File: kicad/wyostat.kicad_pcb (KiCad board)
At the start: 2 copper layers, 99.1 x 99.1 mm, 93 parts, among them J1 24 V AC IN, J10 Y2, J11 G, J12 W1, J13 USB_microAB, J14 W2, J15 Conn_Spare, J16 5V_SEL, J2 OUT1, J3 OUT2, J4 OUT3, J5 I2C_ext1, J6 RH, J7 RC, J8 C, J9 Y1, Q1 BTA204S, Q2 BTA204S, Q3 BTA204S, U1 MOC3063M, U2 MOC3063M, U3 MOC3063M, U4 Wemos-Lolin, U5 MAX17502FATB+T, U6 DS3231N

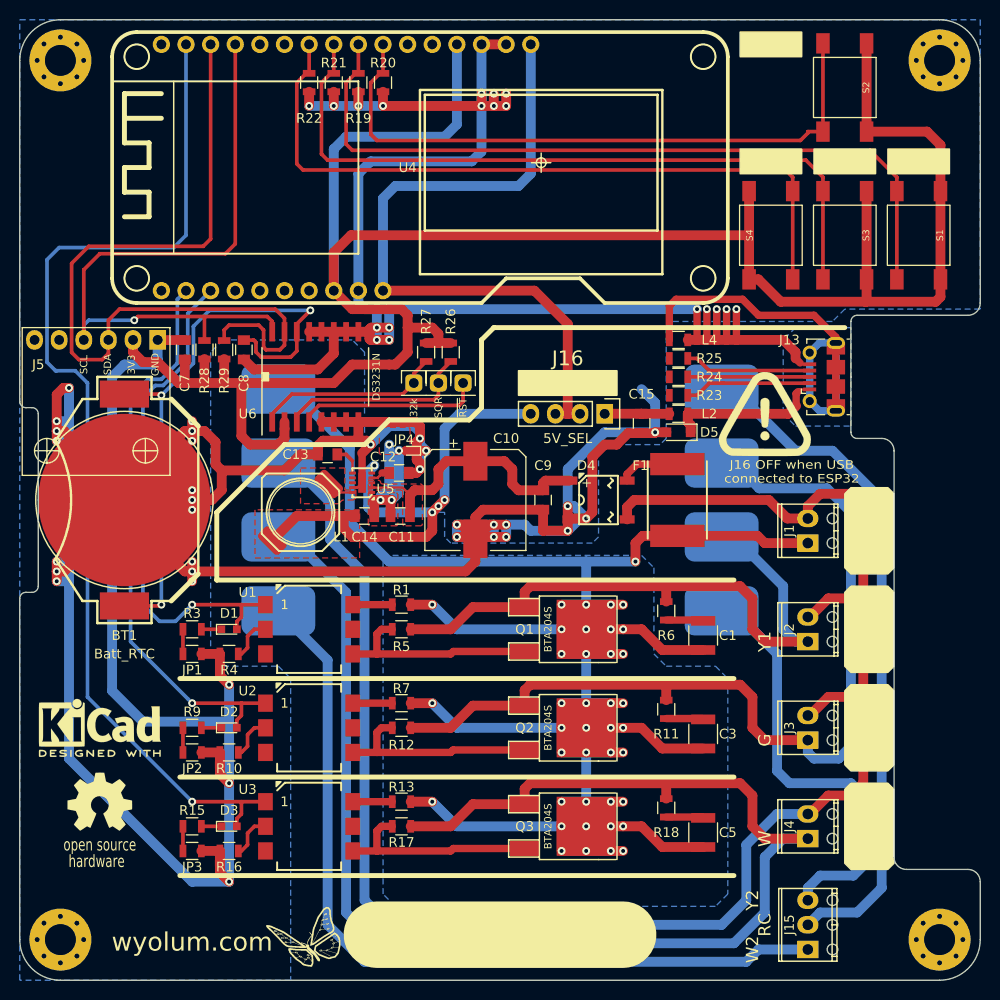
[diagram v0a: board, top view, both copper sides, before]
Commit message: prettified silk legend
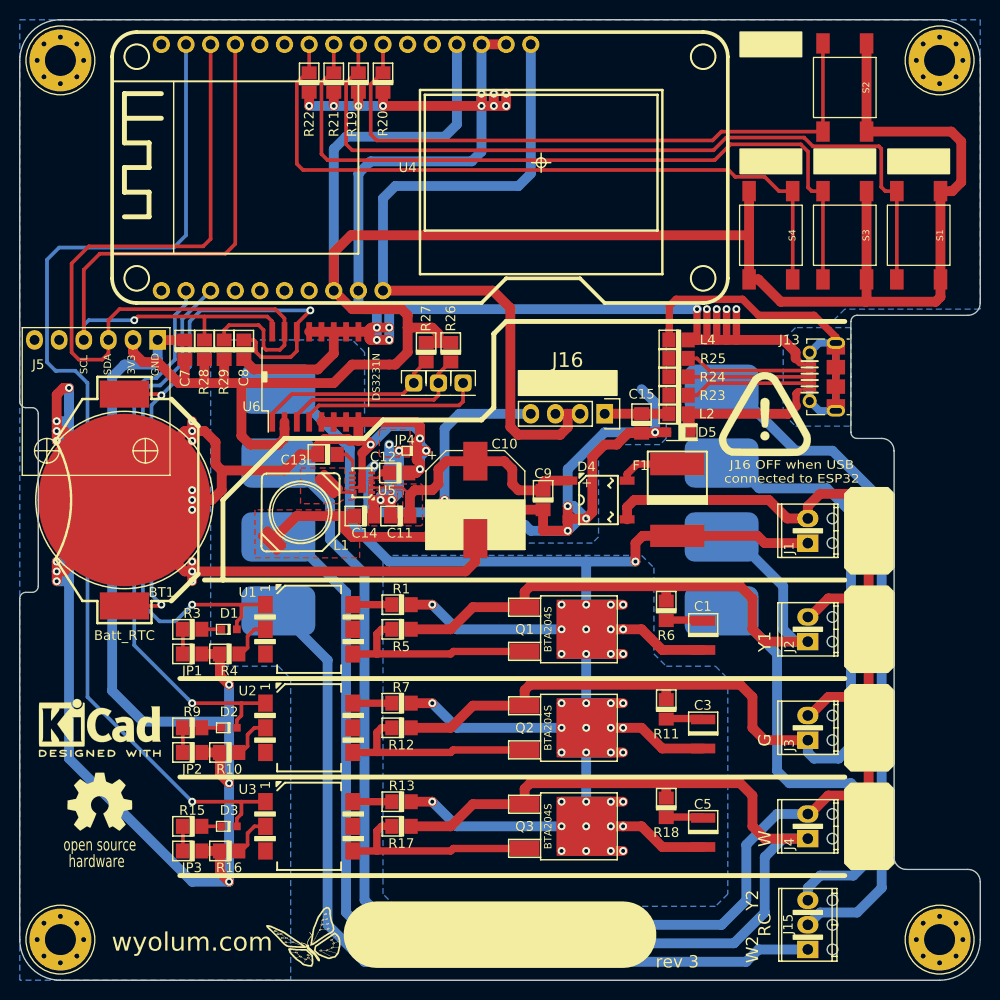
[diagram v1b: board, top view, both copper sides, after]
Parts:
- TP3: value 32k -> 32kHz
- moved J16 3.81 mm to (88.3, 72.4)
- turned C1 to 270 degrees
- turned C11 to 0 degrees
- turned C13 to 0 degrees
- turned C3 to 270 degrees
- turned C5 to 270 degrees
- turned C7 to 270 degrees
- turned JP1 to 0 degrees
- turned JP2 to 0 degrees
- turned JP3 to 0 degrees
- turned JP4 to 0 degrees
- turned L2 to 0 degrees
- turned R1 to 0 degrees
- turned R12 to 0 degrees
- turned R13 to 0 degrees
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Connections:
- C1 pad 1: /24Vac-H -> Net-(C1-Pad1)
- C1 pad 2: Net-(C1-Pad2) -> /24Vac-H
- C11 pad 1: /40VDC -> GND
- C11 pad 2: GND -> /40VDC
- C13 pad 1: /SS -> GND
- C13 pad 2: GND -> /SS
- C3 pad 1: /24Vac-H -> Net-(C3-Pad1)
- C3 pad 2: Net-(C3-Pad2) -> /24Vac-H
- C5 pad 1: /24Vac-H -> Net-(C5-Pad1)
- C5 pad 2: Net-(C5-Pad2) -> /24Vac-H
- C7 pad 1: /3V3 -> GND
- C7 pad 2: GND -> /3V3
- JP1 pad 1: GND -> Net-(JP1-Pad1)
- JP1 pad 2: Net-(JP1-Pad2) -> GND
- JP2 pad 1: GND -> Net-(JP2-Pad1)
- JP2 pad 2: Net-(JP2-Pad2) -> GND
- JP3 pad 1: GND -> Net-(JP3-Pad1)
- JP3 pad 2: Net-(JP3-Pad2) -> GND
- L2 pad 1: /USB+ -> /5V_USB
- L2 pad 2: /5V_USB -> /USB+
- R1 pad 1: /24Vac-H -> Net-(R1-Pad1)
- R1 pad 2: Net-(R1-Pad2) -> /24Vac-H
- R11 pad 2: Net-(C3-Pad2) -> Net-(C3-Pad1)
- R12 pad 1: /OUT2 -> Net-(Q2-Pad3)
- R12 pad 2: Net-(Q2-Pad3) -> /OUT2
- R13 pad 1: /24Vac-H -> Net-(R13-Pad1)
- R13 pad 2: Net-(R13-Pad2) -> /24Vac-H
- R15 pad 1: Net-(JP3-Pad2) -> Net-(JP3-Pad1)
- R17 pad 1: /OUT3 -> Net-(Q3-Pad3)
- R17 pad 2: Net-(Q3-Pad3) -> /OUT3
- R18 pad 2: Net-(C5-Pad2) -> Net-(C5-Pad1)
- R28 pad 1: /3V3 -> /SCL
- R28 pad 2: /SCL -> /3V3
- R29 pad 1: /3V3 -> /SDA
- R29 pad 2: /SDA -> /3V3
- R3 pad 1: Net-(JP1-Pad2) -> Net-(JP1-Pad1)
- R5 pad 1: /OUT1 -> Net-(Q1-Pad3)
- R5 pad 2: Net-(Q1-Pad3) -> /OUT1
- R6 pad 2: Net-(C1-Pad2) -> Net-(C1-Pad1)
- R7 pad 1: /24Vac-H -> Net-(R7-Pad1)
- R7 pad 2: Net-(R7-Pad2) -> /24Vac-H
- R9 pad 1: Net-(JP2-Pad2) -> Net-(JP2-Pad1)
- S4 pad 1: /3V3 -> /SW_M
- S4 pad 2: /SW_M -> /3V3
- S4 pad 3: /3V3 -> /SW_M
- S4 pad 4: /SW_M -> /3V3
- U1 pad 6: Net-(R1-Pad2) -> Net-(R1-Pad1)
- U2 pad 6: Net-(R7-Pad2) -> Net-(R7-Pad1)
- U3 pad 6: Net-(R13-Pad2) -> Net-(R13-Pad1)
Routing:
- net /5V: track 71.4 -> 75.8 mm
- net Net-(R7-Pad2): track 4.07 -> 0.00 mm
- net Net-(R7-Pad1): track 0.00 -> 4.07 mm
- net Net-(R13-Pad2): track 4.07 -> 0.00 mm
- net Net-(R13-Pad1): track 0.00 -> 4.07 mm
- net Net-(R1-Pad2): track 4.07 -> 0.00 mm
- net Net-(R1-Pad1): track 0.00 -> 4.07 mm
- net /3V3: track 229.9 -> 233.8 mm
- net Net-(C3-Pad2): track 3.85 -> 0.00 mm
- net Net-(C3-Pad1): track 0.00 -> 3.85 mm
- net Net-(C1-Pad2): track 3.85 -> 0.00 mm
- net Net-(C1-Pad1): track 0.00 -> 3.85 mm
- net Net-(C5-Pad2): track 3.85 -> 0.00 mm
- net Net-(C5-Pad1): track 0.00 -> 3.85 mm
- net /24Vac-C: track 182.0 -> 185.0 mm
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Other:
- board text added: "rev 3"

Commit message: prettified
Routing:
- net /24Vac-H: track 284.0 -> 285.7 mm
- net /OUT1: track 65.5 -> 67.2 mm
- net /24Vac-C: track 185.0 -> 186.7 mm
